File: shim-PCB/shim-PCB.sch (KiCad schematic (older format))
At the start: 27 parts, among them J1 ROMI-Encoder, J10 LineSensor, J11 LineSensor, J12 SPI, J13 Ultrasonic., J14 THING, J15 THING, J16 Conn_01x02_Female, J17 i2c, J18 ROMI, J2 ROMI-Encoder, J3 Conn_01x19_Female, J4 ServoAnalog, J5 Conn_01x19_Female, J6 Conn_01x19_Female, J7 ROMI, J8 ROMI, J9 Conn_01x19_Female

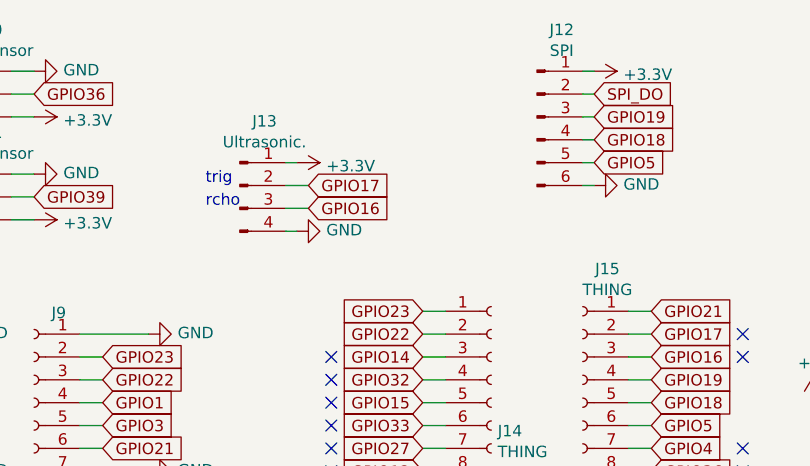
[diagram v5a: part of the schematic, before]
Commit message: Extended board, Added resistor.
#30 #28
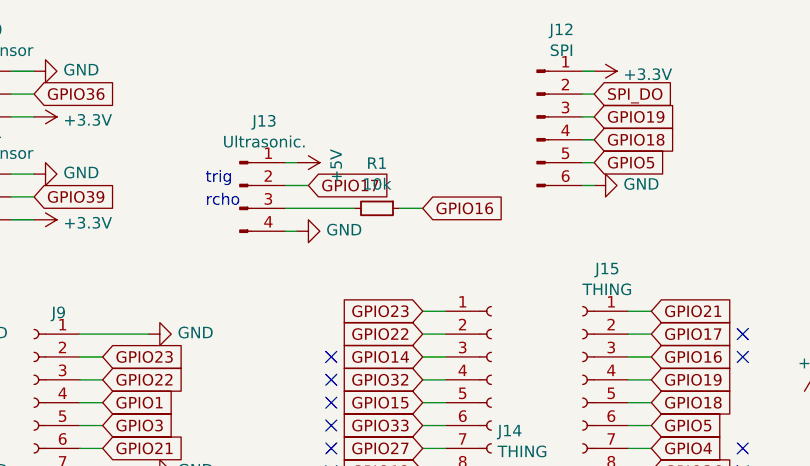
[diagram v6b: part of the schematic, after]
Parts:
- added R1: 10k, Resistor_THT:R_Axial_DIN0204_L3.6mm_D1.6mm_P7.62mm_Horizontal, symbol Device:R_Small
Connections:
- wire segments 159 -> 160
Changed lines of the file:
@@
 Text GLabel 5100 1400 2    50   Input ~ 0
 GPIO17
-Text GLabel 5100 1500 2    50   Input ~ 0
+Text GLabel 5600 1500 2    50   Input ~ 0
 GPIO16
 $Comp
@@
 	3900 1550 3800 1550
 $Comp
-L power:+3.3V #PWR0125
-U 1 1 5F0BD500
-P 5050 1300
-F 0 "#PWR0125" H 5050 1150 50  0001 C CNN
-F 1 "+3.3V" V 5065 1428 50  0000 L CNN
-F 2 "" H 5050 1300 50  0001 C CNN
-F 3 "" H 5050 1300 50  0001 C CNN
-	1    5050 1300
-	0    1    1    0
-$EndComp
-$Comp
 L power:GND #PWR0127
 U 1 1 5F0BDC9A
@@
 Wire Wire Line
 	5100 1400 5000 1400
-Wire Wire Line
-	5100 1500 5000 1500
 $Comp
 L Connector:Conn_01x06_Male J12
@@
 	1    0    0    -1
 $EndComp
+$Comp
+L power:+5V #PWR0125
+U 1 1 5F1AA820
+P 5050 1300
+F 0 "#PWR0125" H 5050 1150 50  0001 C CNN
+F 1 "+5V" H 5065 1473 50  0000 C CNN
+F 2 "" H 5050 1300 50  0001 C CNN
+F 3 "" H 5050 1300 50  0001 C CNN
+	1    5050 1300
+	0    1    1    0
+$EndComp
+$Comp
+L Device:R_Small R1
+U 1 1 5F1ADAC2
+P 5400 1500
+F 0 "R1" V 5204 1500 50  0000 C CNN
+F 1 "10k" V 5295 1500 50  0000 C CNN
+F 2 "Resistor_THT:R_Axial_DIN0204_L3.6mm_D1.6mm_P7.62mm_Horizontal" H 5400 1500 50  0001 C CNN
+F 3 "~" H 5400 1500 50  0001 C CNN
+	1    5400 1500
+	0    1    1    0
+$EndComp
+Wire Wire Line
+	5500 1500 5600 1500
+Wire Wire Line
+	5000 1500 5300 1500
 $EndSCHEMATC

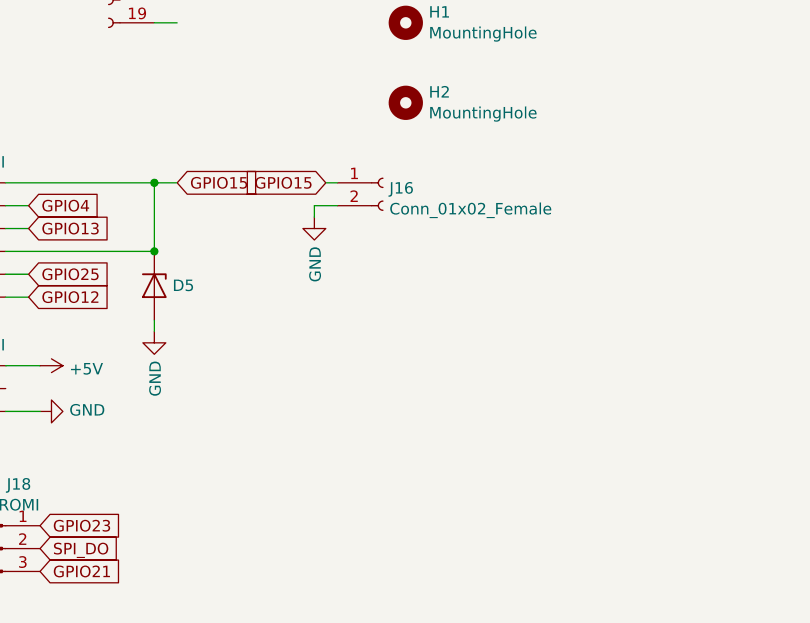
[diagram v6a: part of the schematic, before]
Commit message: 3 pin jumper for motor disable
#29
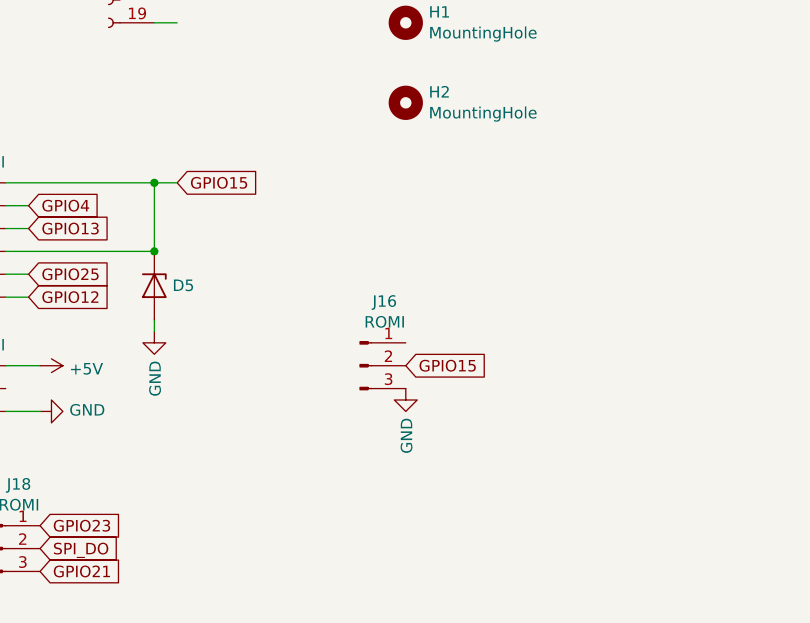
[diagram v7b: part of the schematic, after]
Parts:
- removed J16: Conn_01x02_Female, Connector_PinSocket_2.54mm:PinSocket_1x02_P2.54mm_Vertical, symbol Connector:Conn_01x02_Female
- added J16: ROMI, Connector_PinSocket_2.54mm:PinSocket_1x03_P2.54mm_Vertical, symbol Connector:Conn_01x03_Male
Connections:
- wire segments 160 -> 157
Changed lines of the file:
@@
 Wire Wire Line
 	4200 3850 4100 3850
-$Comp
-L Connector:Conn_01x02_Female J16
-U 1 1 5F30E014
-P 5100 4550
-F 0 "J16" H 5128 4526 50  0000 L CNN
-F 1 "Conn_01x02_Female" H 5128 4435 50  0000 L CNN
-F 2 "Connector_PinSocket_2.54mm:PinSocket_1x02_P2.54mm_Vertical" H 5100 4550 50  0001 C CNN
-F 3 "~" H 5100 4550 50  0001 C CNN
-	1    5100 4550
-	1    0    0    -1
-$EndComp
-Text GLabel 4850 4550 0    50   Input ~ 0
+Text GLabel 5200 5350 2    50   Input ~ 0
 GPIO15
 $Comp
 L power:GND #PWR0135
 U 1 1 5F30EFD3
-P 4800 4700
-F 0 "#PWR0135" H 4800 4450 50  0001 C CNN
-F 1 "GND" V 4805 4572 50  0000 R CNN
-F 2 "" H 4800 4700 50  0001 C CNN
-F 3 "" H 4800 4700 50  0001 C CNN
-	1    4800 4700
-	1    0    0    -1
-$EndComp
-Wire Wire Line
-	4900 4550 4850 4550
-Wire Wire Line
-	4900 4650 4800 4650
-Wire Wire Line
-	4800 4650 4800 4700
+P 5200 5450
+F 0 "#PWR0135" H 5200 5200 50  0001 C CNN
+F 1 "GND" V 5205 5322 50  0000 R CNN
+F 2 "" H 5200 5450 50  0001 C CNN
+F 3 "" H 5200 5450 50  0001 C CNN
+	1    5200 5450
+	1    0    0    -1
+$EndComp
 $Comp
 L Device:D_Zener D6
@@
 Wire Wire Line
 	5000 1500 5300 1500
+$Comp
+L Connector:Conn_01x03_Male J16
+U 1 1 5F1DC6D0
+P 5000 5350
+F 0 "J16" H 5108 5631 50  0000 C CNN
+F 1 "ROMI" H 5108 5540 50  0000 C CNN
+F 2 "Connector_PinSocket_2.54mm:PinSocket_1x03_P2.54mm_Vertical" H 5000 5350 50  0001 C CNN
+F 3 "~" H 5000 5350 50  0001 C CNN
+	1    5000 5350
+	1    0    0    -1
+$EndComp
 $EndSCHEMATC

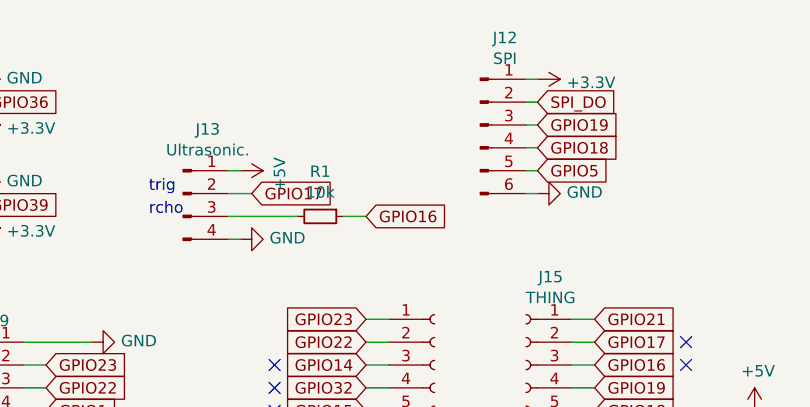
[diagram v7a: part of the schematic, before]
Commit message: Added diode, updated silkscreen. Sleep pin now 1x03
#29
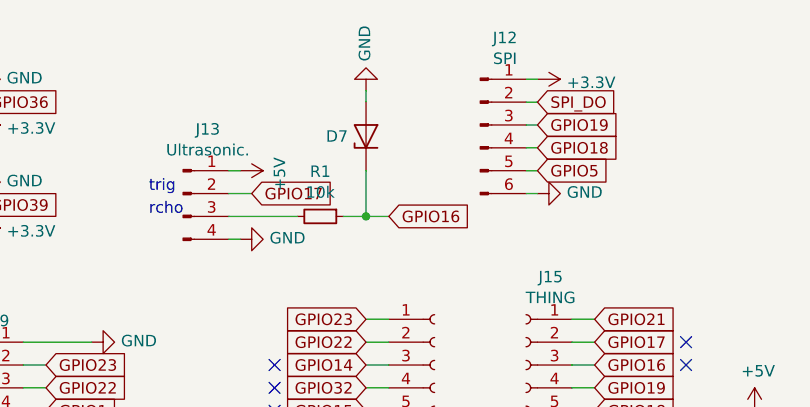
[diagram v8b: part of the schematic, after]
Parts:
- added D7: D_Zener, Diode_THT:D_DO-35_SOD27_P7.62mm_Horizontal, symbol Device:D_Zener
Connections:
- wire segments 157 -> 160
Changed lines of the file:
@@
 Text GLabel 5100 1400 2    50   Input ~ 0
 GPIO17
-Text GLabel 5600 1500 2    50   Input ~ 0
+Text GLabel 5700 1500 2    50   Input ~ 0
 GPIO16
 $Comp
@@
 $EndComp
 Wire Wire Line
-	5500 1500 5600 1500
-Wire Wire Line
 	5000 1500 5300 1500
 $Comp
@@
 	1    0    0    -1
 $EndComp
+$Comp
+L Device:D_Zener D7
+U 1 1 5F1ECB50
+P 5600 1150
+F 0 "D7" V 5600 1229 50  0000 L CNN
+F 1 "D_Zener" V 5645 1229 50  0001 L CNN
+F 2 "Diode_THT:D_DO-35_SOD27_P7.62mm_Horizontal" H 5600 1150 50  0001 C CNN
+F 3 "~" H 5600 1150 50  0001 C CNN
+	1    5600 1150
+	0    -1   -1   0
+$EndComp
+$Comp
+L power:GND #PWR0139
+U 1 1 5F1EDCD3
+P 5600 950
+F 0 "#PWR0139" H 5600 700 50  0001 C CNN
+F 1 "GND" V 5605 822 50  0000 R CNN
+F 2 "" H 5600 950 50  0001 C CNN
+F 3 "" H 5600 950 50  0001 C CNN
+	1    5600 950
+	-1   0    0    1
+$EndComp
+Wire Wire Line
+	5500 1500 5600 1500
+Wire Wire Line
+	5600 1300 5600 1500
+Connection ~ 5600 1500
+Wire Wire Line
+	5600 1500 5700 1500
+Wire Wire Line
+	5600 950  5600 1000
 $EndSCHEMATC
